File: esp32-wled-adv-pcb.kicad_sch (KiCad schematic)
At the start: 30 parts, among them J1 Conn_01x03_Male, J2 Conn_01x03_Male, J3 Conn_01x02_Male, J4 Conn_01x02_Male, Q1 BS170F, SW1 SW_Push, SW2 SW_Push, U1 MT3420C, U2 ESP32-PICO-D4

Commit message: finalize first version of schematic
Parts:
- removed C3: 100n, symbol Device:C
- removed J3, J4: Conn_01x02_Male, symbol Connector:Conn_01x02_Male
- added C9: 100n, symbol Device:C
- added J3: Barrel_Jack, Connector_PinHeader_2.54mm:PinHeader_1x02_P2.54mm_Vertical, symbol Connector:Barrel_Jack
- added R10, R11, R12, R7, R8, R9: 4k7, symbol Device:R
- added RV1, RV2, RV3: 10k, symbol Device:R_Potentiometer
- added SW3: SW_Push, Connector_PinHeader_2.54mm:PinHeader_1x02_P2.54mm_Vertical, symbol Switch:SW_Push
- renumbered C5 to C3, C6 to C4, C7 to C5, C8 to C6, C9 to C7, C4 to C8, R7 to R13, R8 to R14, R9 to R15
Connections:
- net +3V3: now also R11.1, R7.1, R9.1
- net +5V: now also J3.2
- net GND: now also C9.2, J3.1, R10.2, R12.2, R8.2, SW3.1
- net WLED_CTRL_IO13: now reaches R6.2
- net WLED_CTRL_IO13: now also U2.20 (IO13), C9.1, SW3.2
- net WLED_CTRL_IO25: now reaches U2.14 (IO25)
- net WLED_CTRL_IO25: now also RV2.2
- net WLED_CTRL_IO26: now reaches U2.15 (IO26)
- net WLED_CTRL_IO26: now also RV3.2
- net WLED_CTRL_IO14: now reaches U2.17 (IO14)
- net WLED_CTRL_IO14: now also RV1.2
- new net: R9.2, RV2.1
- new net: R10.1, RV2.3
- new net: R7.2, RV1.1
- new net: R8.1, RV1.3
- new net: R11.2, RV3.1
- new net: R12.1, RV3.3
- no-connect marks 31 -> 27
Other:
- note added: "Controls"
- note added: "MCU"
- note added: "brightness"
- note added: "cycle effects ramp brightness cycle palettes"
- note added: "intensity"
- note added: "not on PCB!"
- note added: "speed"
- title: (none) -> ESP32 WLED Advanced PCB
- moved on the sheet: AE1, C3, C4, C5, C6, C7, J1, J2, Q1, R13, R14, R15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

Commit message: assign footprints, refresh pdf of schematic
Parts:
- AE1: footprint (none) -> RF_Antenna:Texas_SWRA117D_2.4GHz_Right
- C1, C2, C3, C4, C5, C6, C7, C8, C9: footprint (none) -> Capacitor_SMD:C_0805_2012Metric
- J1, J2, RV1, RV2, RV3: footprint (none) -> Connector_PinHeader_2.54mm:PinHeader_1x03_P2.54mm_Vertical
- J3: footprint Connector_PinHeader_2.54mm:PinHeader_1x02_P2.54mm_Vertical -> Connector_BarrelJack:BarrelJack_Horizontal; symbol Connector:Barrel_Jack -> Connector:Barrel_Jack_Switch
- L1: footprint (none) -> Footprints:Sumida 252012CDMCD_DS; Part (none) -> 252012DMCD/DS
- Q1: footprint (none) -> Package_TO_SOT_SMD:SOT-23
- R1, R10, R11, R12, R13, R14, R15, R2, R3, R4, R5, R6, R7, R8, R9: footprint (none) -> Resistor_SMD:R_0805_2012Metric
- SW1, SW2: footprint (none) -> Footprints:SW_XUNPU_TS-1077S
- TP1: footprint (none) -> TestPoint:TestPoint_THTPad_D1.0mm_Drill0.5mm
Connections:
- net +5V: now also J3.1; no longer J3.2
- net GND: now also J3.2; no longer J3.1
- no-connect marks 27 -> 28

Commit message: finalize Rev 1
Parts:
- removed TP1: 0.6V, TestPoint:TestPoint_THTPad_D1.0mm_Drill0.5mm, symbol Connector:TestPoint
- added C1: 22µ, Capacitor_SMD:C_0805_2012Metric, symbol Device:C
- added C10, C13, C2: 100n, Capacitor_SMD:C_0805_2012Metric, symbol Device:C
- added C14: 22p, Capacitor_SMD:C_0805_2012Metric, symbol Device:C
- added F1: 5A, Fuse:Fuseholder_Cylinder-5x20mm_Stelvio-Kontek_PTF78_Horizontal_Open, symbol Device:Fuse
- added H1, H2, H3, H4: MountingHole, MountingHole:MountingHole_3.2mm_M3_DIN965, symbol Mechanical:MountingHole
- added J4: Screw_Terminal_01x02, Footprints:KF103-5.0-2P, symbol Connector:Screw_Terminal_01x02
- added J5: Conn_01x02, Connector_PinHeader_2.54mm:PinHeader_1x02_P2.54mm_Vertical, symbol Connector_Generic:Conn_01x02
- added R2: 4k7, Resistor_SMD:R_0805_2012Metric, symbol Device:R
- added SW4: SW_SPST, symbol Switch:SW_SPST
- C12: renamed from C1; value 22µ -> 10µ
- C4: renamed from C3; value 1µ -> 10µ
- J2: footprint Connector_PinHeader_2.54mm:PinHeader_1x03_P2.54mm_Vertical -> Footprints:KF103-5.0-3P; symbol Connector:Conn_01x03_Male -> Connector:Screw_Terminal_01x03
- J3: symbol Connector:Barrel_Jack_Switch -> Connector:Barrel_Jack
- RV1, RV2, RV3: footprint Connector_PinHeader_2.54mm:PinHeader_1x03_P2.54mm_Vertical -> Footprints:Potentiometer_Bourns_PDB181-K415K-x
- SW3: footprint Connector_PinHeader_2.54mm:PinHeader_1x02_P2.54mm_Vertical -> (none)
- renumbered C9 to C11, C2 to C3, C4 to C5, C5 to C6, C6 to C7, C7 to C8, C8 to C9, R9 to R10, R10 to R11, R11 to R12, R12 to R13, R13 to R14, R14 to R15, R15 to R16, R2 to R3, R3 to R4, R4 to R5, R5 to R6, R6 to R7, R7 to R8, R8 to R9
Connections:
- net +3V3: now also C10.1, C14.1
- net +5V: now also C1.2, C13.2, C2.1, F1.1, R2.1; no longer J3.1, U1.1 (EN)
- net GND: now also J3.1, C1.1, C10.2, C13.1, C2.2, J4.1 (Pin_1), J5.1 (Pin_1); no longer J3.2
- net WLED_CTRL_IO13: now also J5.2 (Pin_2)
- net WLED_CTRL_IO14: now also RV3.2; no longer RV1.2
- net WLED_CTRL_IO25: now also RV1.2; no longer RV2.2
- net WLED_CTRL_IO26: now also RV2.2; no longer RV3.2
- net at R4.2, R5.1, U1.6 (FB): now also C14.2
- net LNA: now reaches AE1.1 (A), U2.2 (LNA_IN)
- new net: R2.2, U1.1 (EN)
- new net: J3.2, SW4.1 (A)
- new net +5Vin: F1.2, J4.2 (Pin_2), SW4.2 (B)
- no-connect marks 28 -> 27
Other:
- note added: "0.6V"
- note added: "opt."
- moved on the sheet: C12, C4, C5, C6, C7, C8, C9, J1, L1, R10, R11, R12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

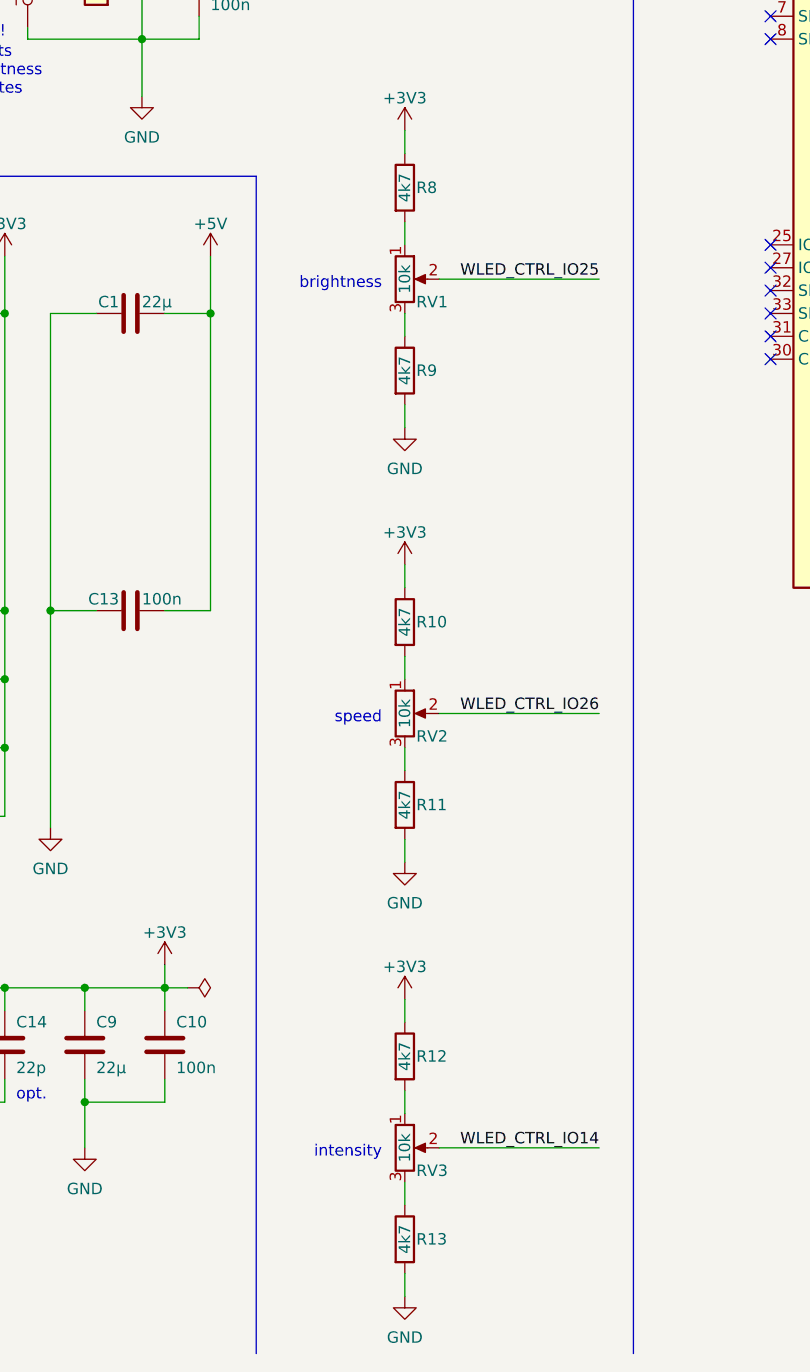
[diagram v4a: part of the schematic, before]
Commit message: change series resistor values for potentiometers
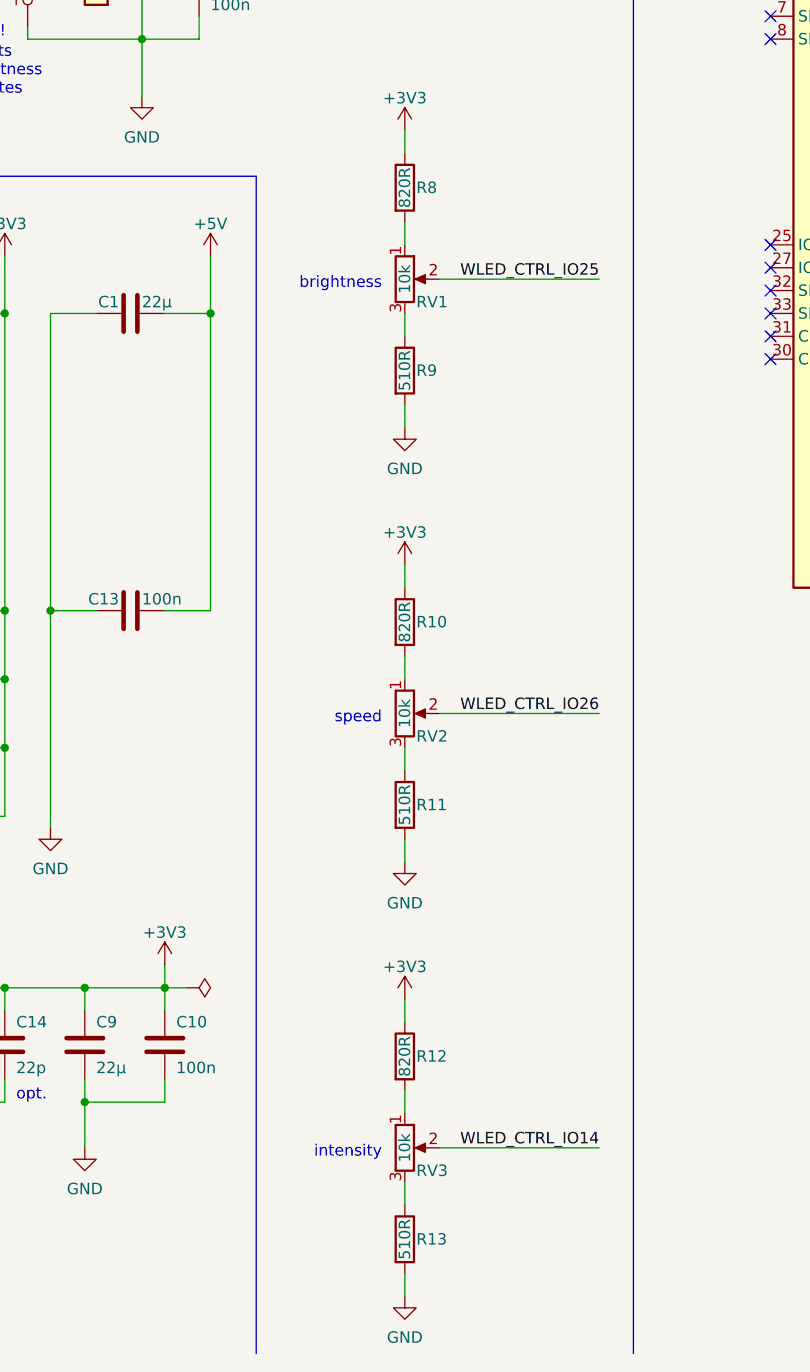
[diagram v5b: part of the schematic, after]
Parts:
- R10, R12, R8: value 4k7 -> 820R
- R11, R13, R9: value 4k7 -> 510R
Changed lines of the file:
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@@
       (effects (font (size 1.27 1.27)) (justify left))
     )
-    (property "Value" "4k7" (id 1) (at 121.92 87.63 90))
+    (property "Value" "510R" (id 1) (at 121.92 87.63 90))
     (property "Footprint" "Resistor_SMD:R_0805_2012Metric" (id 2) (at 120.142 87.63 90)
       (effects (font (size 1.27 1.27)) hide)
@@
       (effects (font (size 1.27 1.27)) (justify left))
     )
-    (property "Value" "4k7" (id 1) (at 121.92 163.83 90))
+    (property "Value" "820R" (id 1) (at 121.92 163.83 90))
     (property "Footprint" "Resistor_SMD:R_0805_2012Metric" (id 2) (at 120.142 163.83 90)
       (effects (font (size 1.27 1.27)) hide)
@@
       (effects (font (size 1.27 1.27)) (justify left))
     )
-    (property "Value" "4k7" (id 1) (at 121.92 67.31 90))
+    (property "Value" "820R" (id 1) (at 121.92 67.31 90))
     (property "Footprint" "Resistor_SMD:R_0805_2012Metric" (id 2) (at 120.142 67.31 90)
       (effects (font (size 1.27 1.27)) hide)
@@
       (effects (font (size 1.27 1.27)) (justify left))
     )
-    (property "Value" "4k7" (id 1) (at 121.92 115.57 90))
+    (property "Value" "820R" (id 1) (at 121.92 115.57 90))
     (property "Footprint" "Resistor_SMD:R_0805_2012Metric" (id 2) (at 120.142 115.57 90)
       (effects (font (size 1.27 1.27)) hide)
@@
       (effects (font (size 1.27 1.27)) (justify left))
     )
-    (property "Value" "4k7" (id 1) (at 121.92 184.15 90))
+    (property "Value" "510R" (id 1) (at 121.92 184.15 90))
     (property "Footprint" "Resistor_SMD:R_0805_2012Metric" (id 2) (at 120.142 184.15 90)
       (effects (font (size 1.27 1.27)) hide)
@@
       (effects (font (size 1.27 1.27)) (justify left))
     )
-    (property "Value" "4k7" (id 1) (at 121.92 135.89 90))
+    (property "Value" "510R" (id 1) (at 121.92 135.89 90))
     (property "Footprint" "Resistor_SMD:R_0805_2012Metric" (id 2) (at 120.142 135.89 90)
       (effects (font (size 1.27 1.27)) hide)
@@
     )
     (path "/7ad2978b-fc4d-4eb5-b142-0ab2628c7b08"
-      (reference "R8") (unit 1) (value "4k7") (footprint "Resistor_SMD:R_0805_2012Metric")
+      (reference "R8") (unit 1) (value "820R") (footprint "Resistor_SMD:R_0805_2012Metric")
     )
     (path "/568d0beb-be3c-42db-a816-bc4900ed0286"
-      (reference "R9") (unit 1) (value "4k7") (footprint "Resistor_SMD:R_0805_2012Metric")
+      (reference "R9") (unit 1) (value "510R") (footprint "Resistor_SMD:R_0805_2012Metric")
     )
     (path "/7d4c4851-43f2-485d-8a4e-c9f0a3bb68c3"
-      (reference "R10") (unit 1) (value "4k7") (footprint "Resistor_SMD:R_0805_2012Metric")
+      (reference "R10") (unit 1) (value "820R") (footprint "Resistor_SMD:R_0805_2012Metric")
     )
     (path "/f8bb5189-c2a9-4789-abdb-c747c26e216c"
-      (reference "R11") (unit 1) (value "4k7") (footprint "Resistor_SMD:R_0805_2012Metric")
+      (reference "R11") (unit 1) (value "510R") (footprint "Resistor_SMD:R_0805_2012Metric")
     )
     (path "/5bd89390-9fe0-4704-aec8-615253616bc3"
-      (reference "R12") (unit 1) (value "4k7") (footprint "Resistor_SMD:R_0805_2012Metric")
+      (reference "R12") (unit 1) (value "820R") (footprint "Resistor_SMD:R_0805_2012Metric")
     )
     (path "/c882f566-f833-409e-bf24-41e7eb7ec656"
-      (reference "R13") (unit 1) (value "4k7") (footprint "Resistor_SMD:R_0805_2012Metric")
+      (reference "R13") (unit 1) (value "510R") (footprint "Resistor_SMD:R_0805_2012Metric")
     )
     (path "/cd783a6f-0e49-4350-a63c-5ed3749cef58"

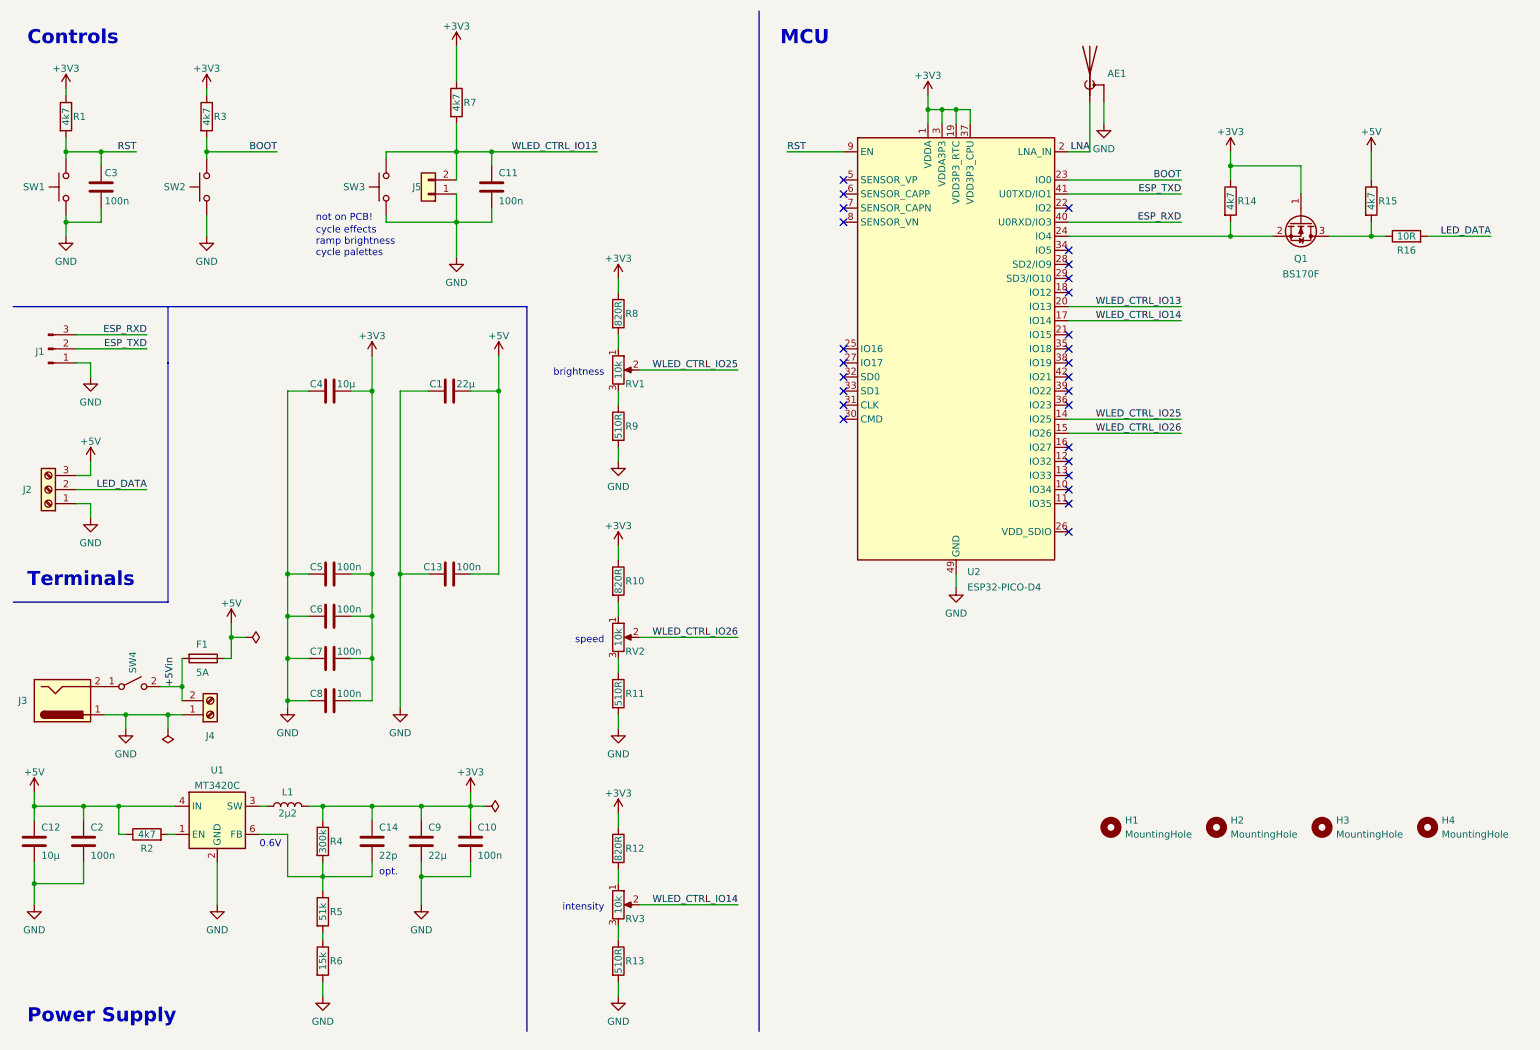
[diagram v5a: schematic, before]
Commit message: change GPIOs for analog inputs and add a second pushbutton
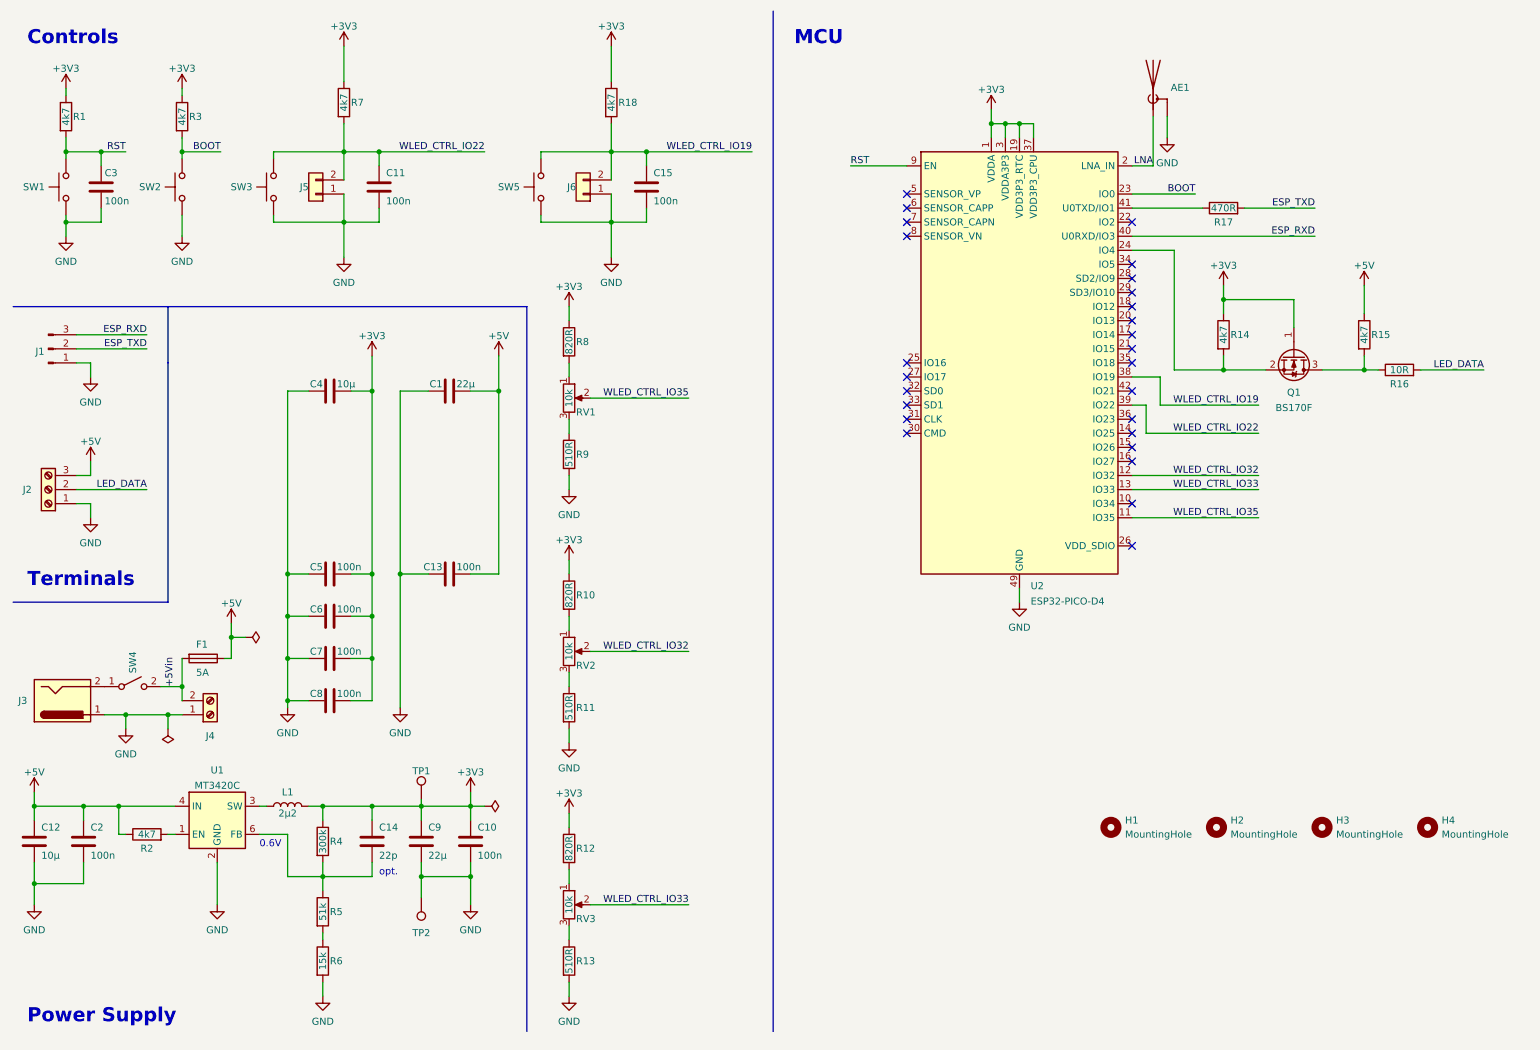
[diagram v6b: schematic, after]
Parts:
- added C15: 100n, Capacitor_SMD:C_0805_2012Metric, symbol Device:C
- added J6: Conn_01x02, Connector_PinHeader_2.54mm:PinHeader_1x02_P2.54mm_Vertical, symbol Connector_Generic:Conn_01x02
- added R17: 470R, Resistor_SMD:R_0805_2012Metric, symbol Device:R
- added R18: 4k7, Resistor_SMD:R_0805_2012Metric, symbol Device:R
- added SW5: SW_Push, symbol Switch:SW_Push
- added TP1: 3V3, TestPoint:TestPoint_THTPad_D1.0mm_Drill0.5mm, symbol Connector:TestPoint
- added TP2: GND, TestPoint:TestPoint_THTPad_D1.0mm_Drill0.5mm, symbol Connector:TestPoint
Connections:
- net +3V3: now also R18.1, TP1.1
- net ESP_TXD: now also R17.2; no longer U2.41 (U0TXD/IO1)
- net GND: now also C15.2, J6.1 (Pin_1), SW5.1, TP2.1
- net WLED_CTRL_IO35: now reaches U2.11 (IO35)
- net WLED_CTRL_IO35: now also RV1.2
- net WLED_CTRL_IO32: now reaches U2.12 (IO32)
- net WLED_CTRL_IO32: now also RV2.2
- net WLED_CTRL_IO33: now reaches U2.13 (IO33)
- net WLED_CTRL_IO33: now also RV3.2
- net WLED_CTRL_IO19: now reaches U2.38 (IO19)
- net WLED_CTRL_IO19: now also C15.1, J6.2 (Pin_2), R18.2, SW5.2
- net WLED_CTRL_IO22: now reaches U2.39 (IO22)
- net WLED_CTRL_IO22: now also C11.1, J5.2 (Pin_2), R7.2, SW3.2
- removed net WLED_CTRL_IO13: C11.1, J5.2 (Pin_2), R7.2, SW3.2, U2.20 (IO13)
- net WLED_CTRL_IO14: no longer names the net of U2.17 (IO14)
- net WLED_CTRL_IO14: no longer RV3.2
- net WLED_CTRL_IO25: no longer names the net of U2.14 (IO25)
- net WLED_CTRL_IO25: no longer RV1.2
- net WLED_CTRL_IO26: no longer names the net of U2.15 (IO26)
- net WLED_CTRL_IO26: no longer RV2.2
- new net: R17.1, U2.41 (U0TXD/IO1)
- no-connect marks 27 -> 26
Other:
- note removed: "brightness"
- note removed: "cycle effects ramp brightness cycle palettes"
- note removed: "intensity"
- note removed: "not on PCB!"
- note removed: "speed"
- moved on the sheet: AE1, C11, J5, Q1, R10, R11, R12, R13, R14, R15, R16, R3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
